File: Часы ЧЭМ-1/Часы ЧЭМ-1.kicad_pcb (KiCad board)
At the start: 2 copper layers, 102 x 131.5 mm, 65 parts, among them SW1 +, SW2 -, SW3 Corr, SW4 Mode

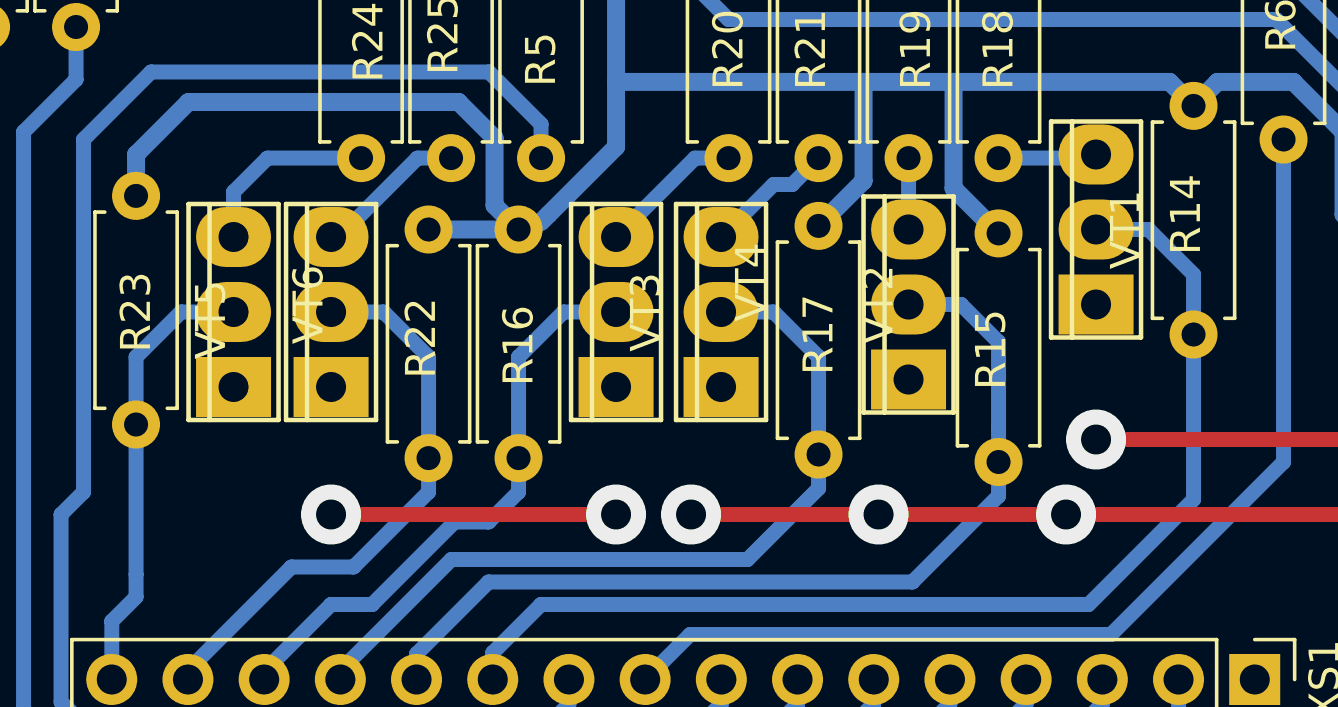
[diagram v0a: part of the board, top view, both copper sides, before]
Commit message: Добавление комментариев на схему, вывод pdf
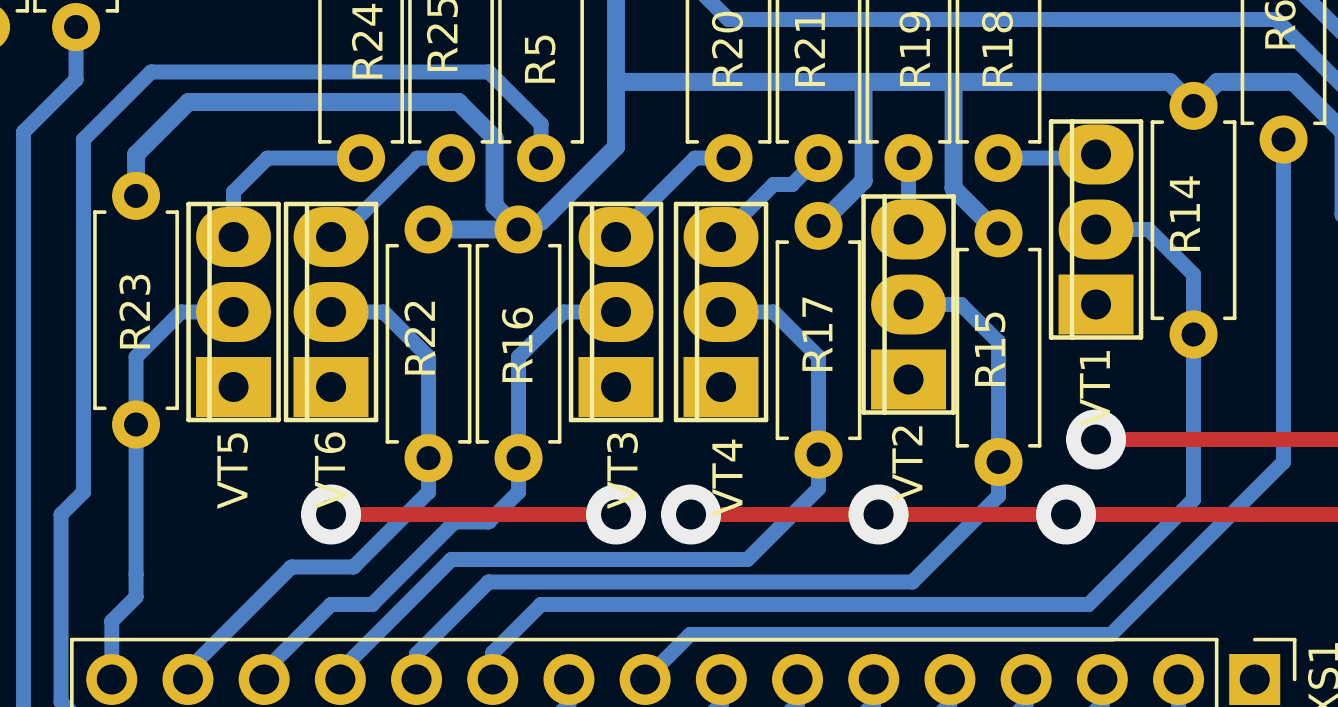
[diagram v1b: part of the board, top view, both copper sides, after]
